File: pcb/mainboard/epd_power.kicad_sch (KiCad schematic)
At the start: 80 parts, among them Q1 AO3401A, Q2 S8050, Q6 AO3400A, Q7 AO3401A, Q8 AO3401A, U10 LGS5148, U11 LM321, U21 INA3221, U22 INA3221, U6 MT9700, U7 MT3608(SOT23-6), U8 MT3608(SOT23-6), U9 LGS5148

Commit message: PCB r0p9
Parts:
- removed C157: 4.7uF/50V, Capacitor_SMD:C_0805_2012Metric, symbol Device:C
- removed D7, D8: B0530WS, Diode_SMD:D_SOD-323, symbol Device:D
- removed R53, R54, R55, R56: 50mR, Resistor_SMD:R_0805_2012Metric, symbol Device:R
- removed U21, U22: INA3221, Package_DFN_QFN:Texas_RGV0016A_VQFN-16-1EP_4x4mm_P0.65mm_EP2.1x2.1mm, symbol Power_Management:INA3221
- removed U7, U8: MT3608(SOT23-6), Package_TO_SOT_SMD:SOT-23-6, symbol symbols:MT3608(SOT23-6)
- added C160, C164: 10uF/10V, Capacitor_SMD:C_0603_1608Metric, symbol Device:C
- added C161, C165, C170, C175: 18pF, Capacitor_SMD:C_0402_1005Metric, symbol Device:C
- added C162, C163, C166, C167, C168, C171, C172, C173, C176, C177: 4.7uF/50V, Capacitor_SMD:C_0805_2012Metric, symbol Device:C
- added C169, C174: 100nF, Capacitor_SMD:C_0402_1005Metric, symbol Device:C
- added D14, D15, D16, D17: 1N5819WS, Diode_SMD:D_SOD-323, symbol Diode:1N5819WS
- added D18, D7: BAT54AW, Package_TO_SOT_SMD:SOT-323_SC-70, symbol Diode:BAT54AW
- added L10, L11, L12, L9: WPN3012H4R7MT, Inductor_SMD:L_Changjiang_FNR3012S, symbol Device:L
- added R70, R71, R75, R80, R82, R86, R90, R91: DNP, Resistor_SMD:R_0402_1005Metric, symbol Device:R
- added R73, R78, R84, R88: 200K/1%, Resistor_SMD:R_0402_1005Metric, symbol Device:R
- added R74, R79: 7.5K/1%, Resistor_SMD:R_0402_1005Metric, symbol Device:R
- added R85, R89: 5.1K/1%, Resistor_SMD:R_0402_1005Metric, symbol Device:R
- added R92, R93, R94, R95: 100K/1%, Resistor_SMD:R_0402_1005Metric, symbol Device:R
- added RV1, RV2, RV3, RV4, RV5, RV6, RV7, RV8: 20K, footprints:Potentiometer_Bourns_TC33X_Vertical, symbol Device:R_Potentiometer_Trim_US
- added U23, U24, U7, U8: LGS6302B5, Package_TO_SOT_SMD:SOT-23-5, symbol Regulator_Switching:LGS6302B5
- added U25, U26: LGS5148, Package_TO_SOT_SMD:TSOT-23-6, symbol symbols:SY8120
- C104, C31, C32: footprint Capacitor_SMD:C_0805_2012Metric -> Capacitor_SMD:C_0603_1608Metric
- C37, C42, C45, C49, C51, C53: footprint Capacitor_SMD:C_1206_3216Metric -> Capacitor_SMD:C_0805_2012Metric
- D1, D2, D3, D4, D5, D6: value B0530WS -> 1N5819WS
- L4, L7: value WPN4020H4R7MT -> WPN3012H4R7MT; footprint Inductor_SMD:L_Changjiang_FNR4020S -> Inductor_SMD:L_Changjiang_FNR3012S
- L5, L6: value FTC201610S4R7MBCA -> WPN3012H4R7MT; footprint Inductor_SMD:L_Murata_DFE201610P -> Inductor_SMD:L_Changjiang_FNR3012S
- R18, R22: value 240K/1% -> 200K/1%
- R19: value 10K/1% -> 5.1K/1%
- R20: value 91K/1% -> 200K/1%
- R21, R29: value 5.1K -> 5.1K/1%
- R23, R25: value 10K/1% -> 7.5K/1%
- R24: value 390K/1% -> 200K/1%
- R26: value 91K/1% -> 100K/1%
- R27: value 27K/1% -> 20K
- R28, R31, R32, R33, R34, R62: value 120K/1% -> 100K/1%
- R30: value 27K/1% -> 5.1K/1%
- R64: value 20K/1% -> 20K
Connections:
- net S4P is gone; now on net VGH: C41.2, C44.2, D2.1 (K), R24.2
- net VPOS is gone; now on net VP1: C48.2
- net +5V_EPD: no longer C31.2, C32.2, L4.1, L5.1, Q1.2 (S), R28.2, R52.1
- net EN_VGL: now also R93.1, R94.2; no longer R31.1, R33.2
- net GND: now also C160.1, C162.1, C163.1, C164.1, C166.1, C167.1, C170.2, C171.2, C172.2, C175.2, C176.2, C177.2, D16.1 (K), D17.1 (K), L11.2, L12.2, R70.1, R71.1, R75.1, R80.1, R84.2, R88.2, RV1.2, RV1.3, RV2.2, RV2.3, RV3.2, RV3.3, RV4.2, RV4.3, U23.2 (GND), U24.2 (GND), U7.2 (GND), U8.2 (GND); no longer R23.1, R25.1
- net VGL: now also R91.1, R94.1, RV8.2, RV8.3; no longer R19.1, R33.1
- net VNEG: no longer C34.1, C47.1, C50.1, C54.2, D4.2 (A), D6.1 (K), R21.1, R26.1, R34.1, U10.2 (GND), U11.2 (V-)
- net at D1.2 (A), L4.2: now also U7.1 (SW)
- net at R32.2: now also D18.2
- net at C40.1, R22.1, R23.2: now also U7.3 (FB)
- net at R31.2: now also D18.1
- net at Q1.3 (D): now also D18.3, D7.3
- net at C41.1, R24.1, R25.2: now also U24.3 (FB)
- net at D2.2 (A), L5.2: now also U24.1 (SW)
- removed net EN_VNEG: R32.1, R34.2, U10.4 (~{SHDN})
- net S1N renamed +5V_EG
- net +5V_EG: now also C32.2, L5.1, U24.5 (IN)
- net S2N renamed +5V_ES
- net +5V_ES: now also C31.2, L4.1, R52.1, C160.2, C164.2, C168.2, C173.2, L10.1, L9.1, U23.5 (IN), U25.5 (IN), U26.5 (IN), U7.5 (IN), U8.5 (IN)
- net S3P renamed VP1
- net SHDN renamed EPD_SHDN
- net EPD_SHDN: now also U23.4 (EN), U24.4 (EN), U7.4 (EN), U8.4 (EN)
- net VBUS renamed +5V2
- net +5V2: now also Q1.2 (S), R28.2
- new net: C169.1, L11.1, U25.6 (SW)
- new net: D7.2, R93.2
- new net: R74.1, R75.2, RV3.1
- new net: D14.2 (A), L9.2, U8.1 (SW)
- new net: C161.1, R73.1, R74.2, U8.3 (FB)
- new net: R85.1, R86.2, RV6.1
- new net: C170.1, R84.1, R85.2, U25.3 (FB)
- new net: R23.1, R70.2, RV1.1
- new net: C174.2, U26.1 (BS)
- new net: C175.1, R88.1, R89.2, U26.3 (FB)
- new net: C174.1, L12.1, U26.6 (SW)
- new net: R79.1, R80.2, RV4.1
- new net: R21.1, R82.2, RV5.1
- new net: R89.1, R90.2, RV7.1
- new net: D15.2 (A), L10.2, U23.1 (SW)
- new net: D7.1, R92.2
- new net: R25.1, R71.2, RV2.1
- new net: R19.1, R91.2, RV8.1
- new net: C165.1, R78.1, R79.2, U23.3 (FB)
- new net: C169.2, U25.1 (BS)
- new net EN_VN1: R31.1, R95.2, U10.4 (~{SHDN})
- new net EN_VN2: R32.1, R33.2, U25.4 (~{SHDN})
- new net EN_VN3: R34.2, R92.1, U26.4 (~{SHDN})
- new net VN1: C34.1, C47.1, C50.1, D4.2 (A), R82.1, R95.1, RV5.2, RV5.3, U10.2 (GND)
- new net VN2: C168.1, C171.1, C172.1, D16.2 (A), R33.1, R86.1, RV6.2, RV6.3, U25.2 (GND)
- new net VN3: C173.1, C176.1, C177.1, C54.2, D17.2 (A), D6.1 (K), R26.1, R34.1, R90.1, RV7.2, RV7.3, U11.2 (V-), U26.2 (GND)
- new net VP2: C161.2, C162.2, C163.2, D14.1 (K), R73.2
- new net VP3: C165.2, C166.2, C167.2, D15.1 (K), R78.2
- no-connect marks 3 -> 0
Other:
- note added: "Gallery1 Gallery3 Spectra6 VGH 27.0V 35.3V 27.0V VGL -20.0V -35.8V -20.0V VN2 - 2.5V -10.0V -11.0V VN1 -12.0V -16.9V -11.2V VN3 -15.0V -24.4V -15.0V VP2 10.0V 10.0V 6.6V VP1 16.0V 16.9V 7.4V VP3 20.0V 24.0V 15.0V"
- note added: "Only populate for non-Lite model"
- moved on the sheet: C104, C31, C32, C33, C34, C35, C36, C37, C38, C39, C40, C41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

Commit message: PCB r0p10 wip
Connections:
- net VCOM renamed -VCOM
- net VGH renamed +VGH
- net VGL renamed -VGL
- net VN1 renamed -VN1
- net VN2 renamed -VN2
- net VN3 renamed -VN3
- net VP1 renamed +VP1
- net VP2 renamed +VP2
- net VP3 renamed +VP3
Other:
- note added: "IS LM321 RATED FOR 30V??"
- moved on the sheet: C52, C54, C56, D5, Q6, Q7, Q8, R26, R27, R62, R63, R64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

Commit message: PCB r0p10
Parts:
- removed C160, C31: 10uF/10V, Capacitor_SMD:C_0603_1608Metric, symbol Device:C
- removed C161, C170, C39, C40: 18pF, Capacitor_SMD:C_0402_1005Metric, symbol Device:C
- removed C162, C163, C168, C171, C172, C34, C43, C47, C48, C50: 4.7uF/50V, Capacitor_SMD:C_0805_2012Metric, symbol Device:C
- removed C169, C36: 100nF, Capacitor_SMD:C_0402_1005Metric, symbol Device:C
- removed D1, D14, D16, D4: 1N5819WS, Diode_SMD:D_SOD-323, symbol Diode:1N5819WS
- removed D18: BAT54AW, Package_TO_SOT_SMD:SOT-323_SC-70, symbol Diode:BAT54AW
- removed L11, L4, L7, L9: WPN3012H4R7MT, Inductor_SMD:L_Changjiang_FNR3012S, symbol Device:L
- removed R20, R22, R73, R84: 200K/1%, Resistor_SMD:R_0402_1005Metric, symbol Device:R
- removed R21, R85: 5.1K/1%, Resistor_SMD:R_0402_1005Metric, symbol Device:R
- removed R23, R74: 7.5K/1%, Resistor_SMD:R_0402_1005Metric, symbol Device:R
- removed R31, R32, R33, R95: 100K/1%, Resistor_SMD:R_0402_1005Metric, symbol Device:R
- removed R52: 10K/1%, Resistor_SMD:R_0402_1005Metric, symbol Device:R
- removed R70, R71, R75, R80, R82, R86, R90, R91: DNP, Resistor_SMD:R_0402_1005Metric, symbol Device:R
- removed RV1, RV2, RV3, RV4, RV5, RV6, RV7, RV8: 20K, footprints:Potentiometer_Bourns_TC33X_Vertical, symbol Device:R_Potentiometer_Trim_US
- removed U10, U25: LGS5148, Package_TO_SOT_SMD:TSOT-23-6, symbol symbols:SY8120
- removed U7, U8: LGS6302B5, Package_TO_SOT_SMD:SOT-23-5, symbol Regulator_Switching:LGS6302B5
- added R13: DNP, Resistor_SMD:R_0402_1005Metric, symbol Device:R
- R18: value 200K/1% -> 240K/1%
- R19: value 5.1K/1% -> 10K/1%
- R24: value 200K/1% -> 680K/1%
- R25: value 7.5K/1% -> 39K/1%
- R27, R64: value 20K -> 20K/1%
- R78: value 200K/1% -> 150K/1%
- R79: value 7.5K/1% -> 13K/1%
- R88: value 200K/1% -> 390K/1%
- R89: value 5.1K/1% -> 22K/1%
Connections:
- net -VN3 is gone; now on net -VN: C173.1, C176.1, C177.1, C54.2, D17.2 (A), D6.1 (K), R26.1, R34.1, U11.2 (V-), U26.2 (GND)
- net VNEG is gone; now on net -VN: R62.2
- net +5V2: no longer Q1.2 (S), R28.2
- net +5V_EPD: now also Q1.2 (S), R28.2
- net -VGL: now also R19.1
- net GND: now also R25.1, R79.1
- net -VN: now reaches R89.1
- net at C41.1, R24.1, R25.2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: now also R13.1
- net +VP3 renamed +VP
- net EN_VN3 renamed EN_VN
- net EPD_VCOM_PWM renamed VCOM_DAC
- new net VGH_DAC: R13.2
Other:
- note removed: "Gallery1 Gallery3 Spectra6 VGH 27.0V 35.3V 27.0V VGL -20.0V -35.8V -20.0V VN2 - 2.5V -10.0V -11.0V VN1 -12.0V -16.9V -11.2V VN3 -15.0V -24.4V -15.0V VP2 10.0V 10.0V 6.6V VP1 16.0V 16.9V 7.4V VP3 20.0V 24.0V 15.0V"
- note removed: "IS LM321 RATED FOR 30V??"
- note removed: "Only populate for non-Lite model"
- moved on the sheet: C104, C164, C165, C166, C167, C173, C174, C175, C176, C177, C32, C33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

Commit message: PCB r0p11
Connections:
- net +5V2 renamed +5V_DCDC
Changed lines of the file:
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@@
 		(on_board yes)
 		(dnp no)
-		(fields_autoplaced yes)
 		(property "Reference" "#PWR054"
 			(at 45.72 43.18 0)
@@
 			)
 		)
-		(property "Value" "+5V2"
-			(at 45.72 34.29 0)
+		(property "Value" "+5V_DCDC"
+			(at 41.91 34.29 0)
 			(effects
 				(font
 					(size 1.27 1.27)
 				)
+				(justify left)
 			)
 		)

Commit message: PCB r0p13
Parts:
- removed C164: 10uF/10V, Capacitor_SMD:C_0603_1608Metric, symbol Device:C
- removed D7: BAT54AW, Package_TO_SOT_SMD:SOT-323_SC-70, symbol Diode:BAT54AW
- added C160: 100nF/50V, Capacitor_SMD:C_0402_1005Metric, symbol Device:C
- added C17: 22uF/10V, Capacitor_SMD:C_0805_2012Metric, symbol Device:C
- added D1, D4: 1N5819WS, Diode_SMD:D_SOD-323, symbol Diode:1N5819WS
- C104, C32: value 10uF/10V -> 22uF/10V; footprint Capacitor_SMD:C_0603_1608Metric -> Capacitor_SMD:C_0805_2012Metric; Ref.Price (none) -> 0.0165
- C165, C175, C38, C41: value 18pF -> 18pF/50V
- C174, C35, C54: value 100nF -> 100nF/50V
- C37, C42, C45, C49, C51, C53: value 47uF/10V -> 22uF/10V
- C52: value 220nF -> 470nF/25V
- C56: value 1uF -> 4.7uF/6.3V
- R13: value DNP -> 100K/1%
- R24: value 680K/1% -> 390K/1%
- R25: value 39K/1% -> 22K/1%
- R27, R64: value 20K/1% -> 22K/1%
- R63, R66: value 51R -> 33R/1%
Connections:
- net +5V_EPD: now also U11.5 (V+), C160.2
- net +5V_ES: now also C17.2
- net GND: now also C160.1, C17.1; no longer U11.5 (V+)
- net at R93.2: now also D4.1 (K)
- net at Q1.3 (D): now also D1.2 (A), D4.2 (A)
- net at R92.2: now also D1.1 (K)
- net EPD_SHDN renamed EPD_POS_EN
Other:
- note added: "Range: 0V ~ -2.7V"
- note removed: "Range: -0.89V ~ -3.43V"
- company: (none) -> Copyright 2025 Wenting Zhang
- title: (none) -> Glider
- moved on the sheet: C52, C54, C56, D5, Q6, Q7, Q8, R17, R26, R27, R34, R62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

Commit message: PCB r1.1
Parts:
- added C171: 100nF/50V, Capacitor_SMD:C_0402_1005Metric, symbol Device:C
- C104, C17, C32, C37, C42, C45, C49, C51, C53: LCSC (none) -> C29277
- C160, C174, C35, C54: LCSC (none) -> C131394
- C165, C175, C38, C41: LCSC (none) -> C106202
- C166, C167, C173, C176, C177, C33, C44, C46: LCSC (none) -> C6119903
- C52: LCSC (none) -> C6119801
- C56: LCSC (none) -> C307423
- D1, D15, D17, D2, D3, D4, D5, D6: footprint Diode_SMD:D_SOD-323 -> footprints:D_SOD-323_Alt; LCSC (none) -> C488405
- L10, L12, L5, L6: LCSC (none) -> C98357
- Q1, Q7, Q8: LCSC (none) -> C347476
- Q2: LCSC (none) -> C444723
- Q6: LCSC (none) -> C347475
- R13, R26, R28, R34, R62, R92, R93, R94: LCSC (none) -> C25741
- R17, R19, R65: LCSC (none) -> C25744
- R18: LCSC (none) -> C64043
- R24, R88: LCSC (none) -> C25782
- R25, R27, R64, R89: LCSC (none) -> C25768
- R29, R30: LCSC (none) -> C25905
- R63, R66: LCSC (none) -> C25105
- R78: LCSC (none) -> C25755
- R79: LCSC (none) -> C25754
- U11: LCSC (none) -> C9405
- U23, U24: LCSC (none) -> C5123975
- U26, U9: value LGS5148 -> LGS5145; LCSC (none) -> C5123971
- U6: LCSC (none) -> C89855
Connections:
- net GND: now also C171.1
- net VCOM_MEA: now also C171.2
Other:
- company: Copyright 2025 Wenting Zhang -> Copyright 2025 Modos Tech Inc
- moved on the sheet: C32, C41, C44, D2, L5, R13, R24, R25, U24

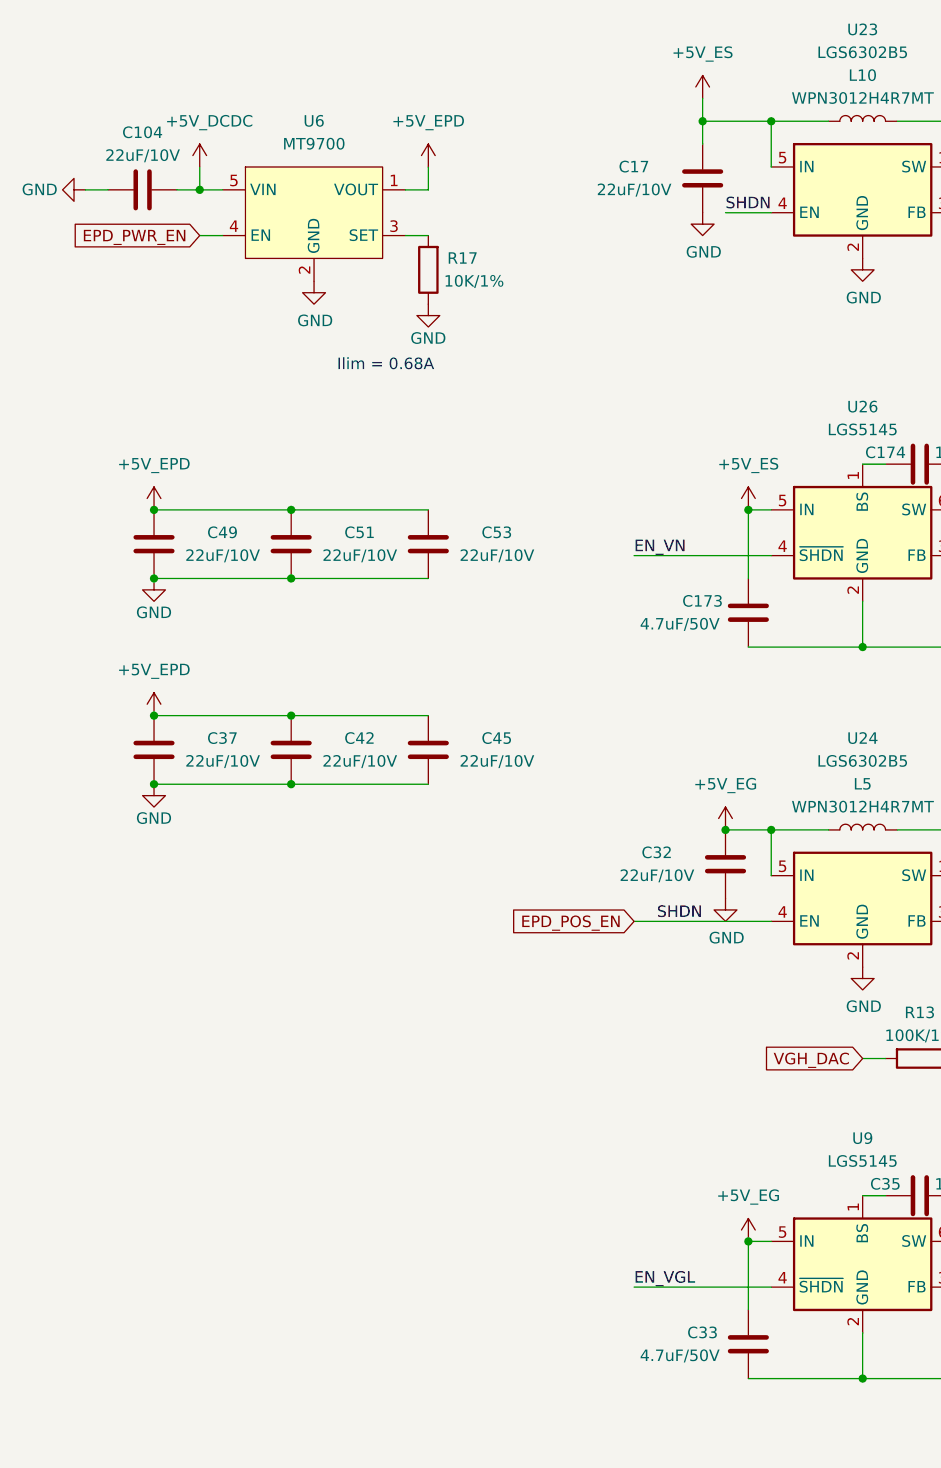
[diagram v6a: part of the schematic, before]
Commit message: PCB r1.2, new adapters
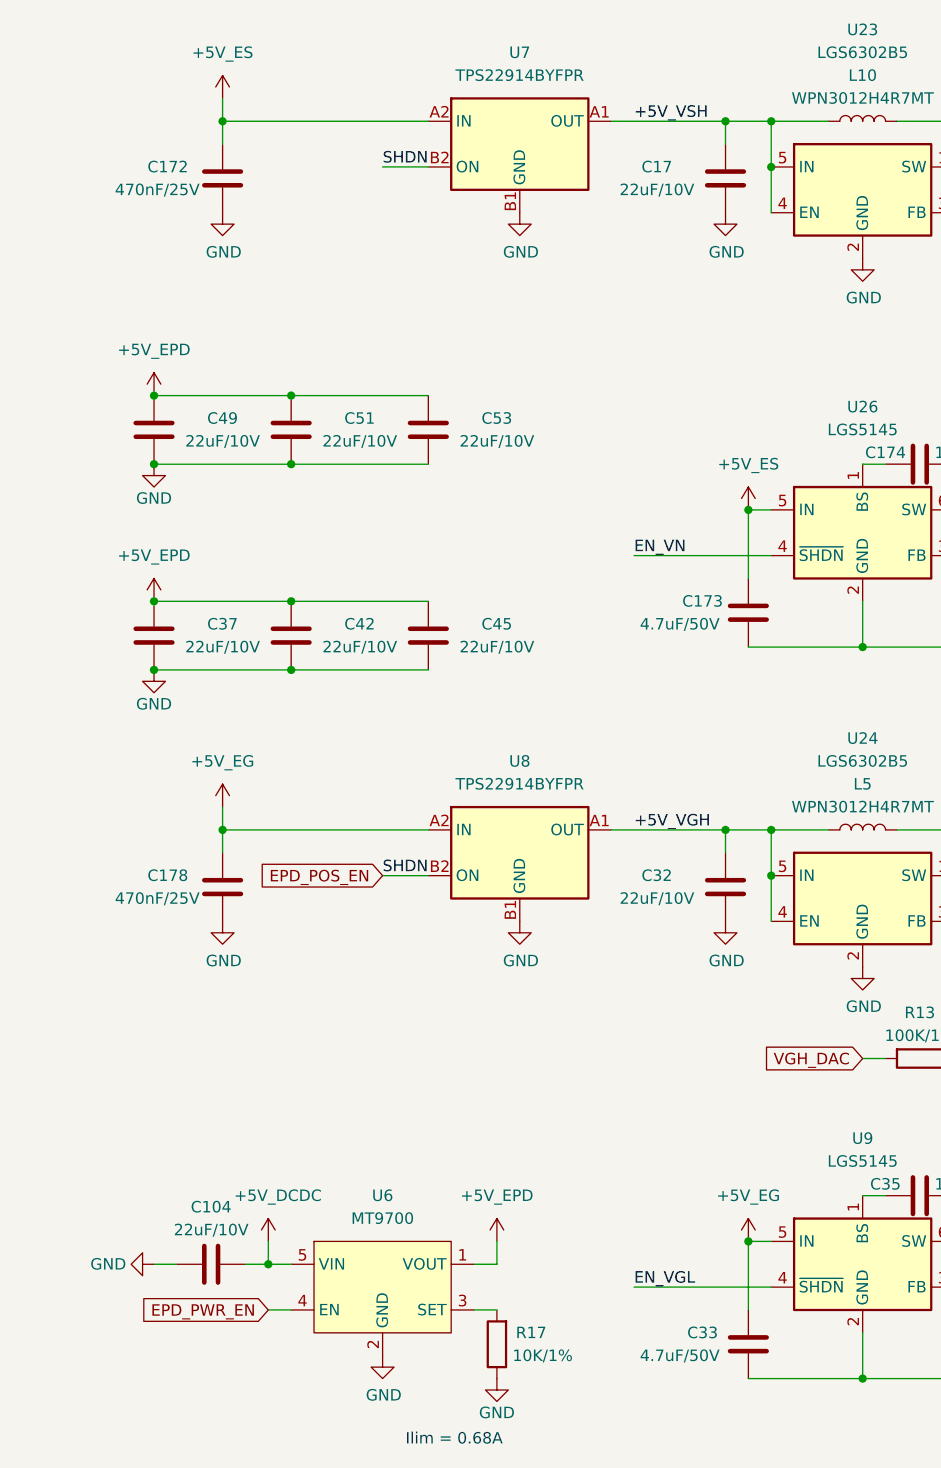
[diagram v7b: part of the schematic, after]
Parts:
- added C172, C178: 470nF/25V, Capacitor_SMD:C_0402_1005Metric, symbol Device:C
- added U7, U8: TPS22914BYFPR, Package_CSP:WLCSP-4-X1-WLB0909-4_0.89x0.89mm_P0.5mm, symbol Power_Management:AP22913CN4
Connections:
- net +5V_EG: now also C178.1, U8.A2 (IN); no longer C32.2, L5.1, U24.5 (IN)
- net +5V_ES: now also C172.1, U7.A2 (IN); no longer C17.2, L10.1, U23.5 (IN)
- net EPD_POS_EN: now also U7.B2 (ON), U8.B2 (ON); no longer U23.4 (EN), U24.4 (EN)
- net GND: now also C172.2, C178.2, U7.B1 (GND), U8.B1 (GND)
- new net +5V_VGH: C32.2, L5.1, U24.4 (EN), U24.5 (IN), U8.A1 (OUT)
- new net +5V_VSH: C17.2, L10.1, U23.4 (EN), U23.5 (IN), U7.A1 (OUT)
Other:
- moved on the sheet: C104, C17, C32, C37, C42, C45, C49, C51, C53, R17, U6
